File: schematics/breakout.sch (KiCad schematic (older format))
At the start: 6 parts, among them P1 RPI_HEADER, P2 CONN_01X03, P3 CONN_01X03, P4 CONN_01X03, P5 CONN_01X03, P6 CONN_01X02

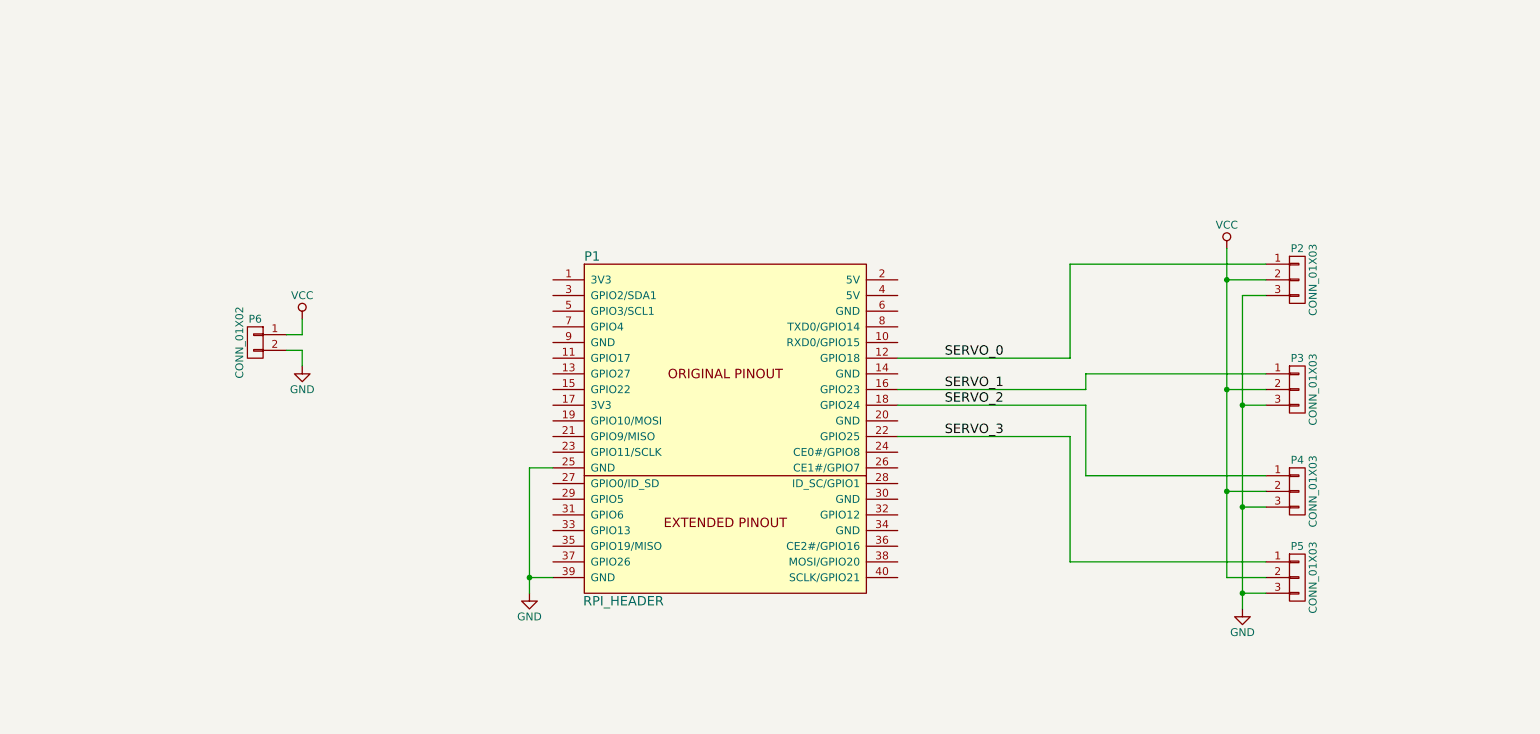
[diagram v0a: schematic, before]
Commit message: Laying out breakout board
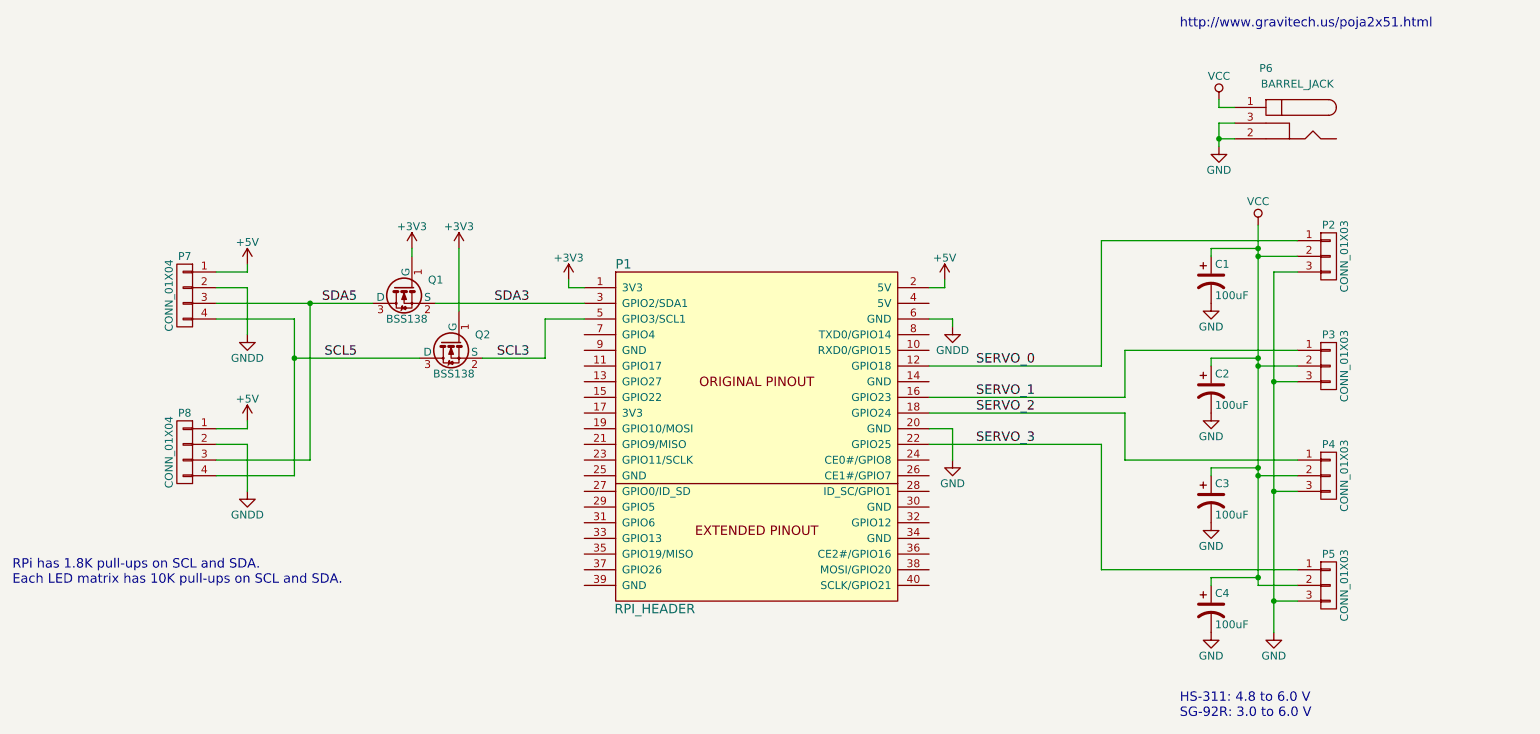
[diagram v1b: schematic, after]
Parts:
- removed P6: CONN_01X02, symbol CONN_01X02
- added C1, C2, C3, C4: 100uF, Capacitors_ThroughHole:C_Radial_D5_L11_P2, symbol CP1
- added P6: BARREL_JACK, Connect:BARREL_JACK, symbol BARREL_JACK
- added P7, P8: CONN_01X04, Pin_Headers:Pin_Header_Straight_1x04, symbol CONN_01X04
- added Q1, Q2: BSS138, TO_SOT_Packages_SMD:SOT-23, symbol BSS138
- P1: footprint (none) -> Pin_Headers:Pin_Header_Straight_2x20
- P2, P3, P4, P5: footprint (none) -> Pin_Headers:Pin_Header_Straight_1x03
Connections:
- net GND: now also P1.20 (GND), C1.2, C2.2, C3.2, C4.2, P6.2, P6.3; no longer P1.25 (GND), P1.39 (GND)
- net VCC: now also C1.1, C2.1, C3.1, C4.1, P6.1
- net +3V3: now reaches P1.1 (3V3)
- net +3V3: now also Q1.1 (G), Q2.1 (G)
- net +5V: now reaches P1.2 (5V)
- net +5V: now also P7.1 (P1), P8.1 (P1)
- net SDA3: now reaches P1.3 (GPIO2/SDA1)
- net SDA3: now also Q1.2 (S)
- net SCL3: now reaches P1.5 (GPIO3/SCL1)
- net SCL3: now also Q2.2 (S)
- net GNDD: now reaches P1.6 (GND)
- net GNDD: now also P7.2 (P2), P8.2 (P2)
- new net SCL5: P7.4 (P4), P8.4 (P4), Q2.3 (D)
- new net SDA5: P7.3 (P3), P8.3 (P3), Q1.3 (D)
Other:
- note added: "HS-311: 4.8 to 6.0 V\nSG-92R: 3.0 to 6.0 V"
- note added: "RPi has 1.8K pull-ups on SCL and SDA.\nEach LED matrix has 10K pull-ups on SCL and SDA."
- note added: "http://www.gravitech.us/poja2x51.html"
- moved on the sheet: P1, P2, P3, P4, P5

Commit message: Updated layouts for order
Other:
- note removed: "http://www.gravitech.us/poja2x51.html"
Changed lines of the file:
@@
 	9050 1850 8950 1850
 Connection ~ 8950 1950
-Text Notes 8700 1250 0    60   ~ 0
-http://www.gravitech.us/poja2x51.html
 Wire Wire Line
 	7250 3150 7250 3100
